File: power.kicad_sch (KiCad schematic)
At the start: 37 parts, among them Q1 SIS472DN-T1-GE3, Q2 SIS472DN-T1-GE3, Q3 AO3400A, U6 LM74700QDBVRQ1, U7 SIC431AED-T1-GE3, U8 LM74700QDBVRQ1, U9 TPS564247DRLR

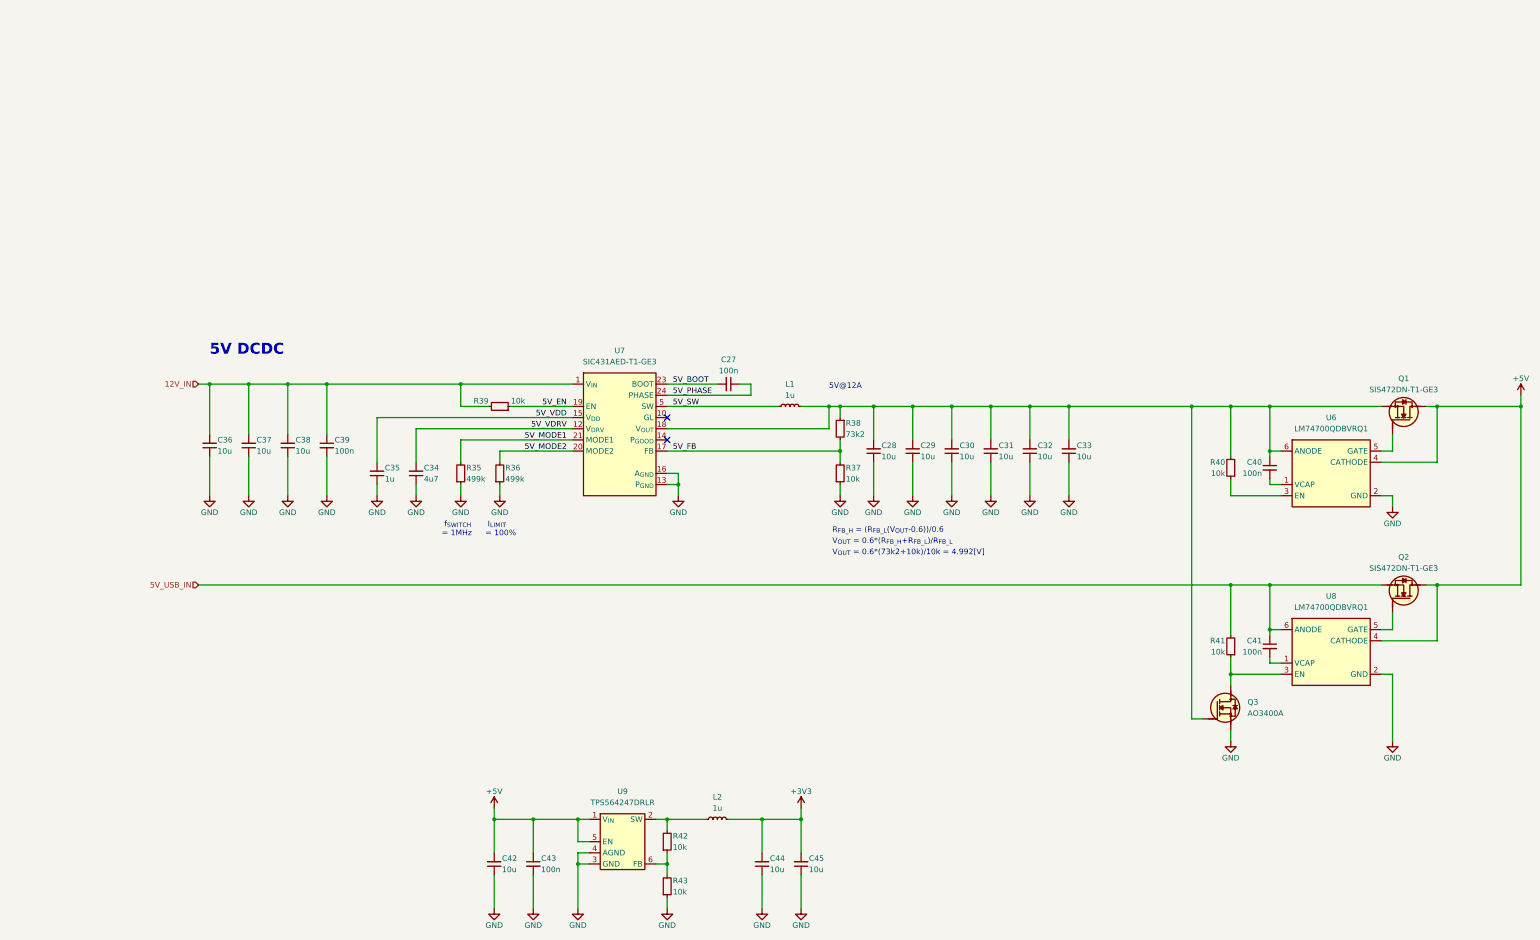
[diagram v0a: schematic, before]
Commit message: [#1] WIP: Refactor schematic
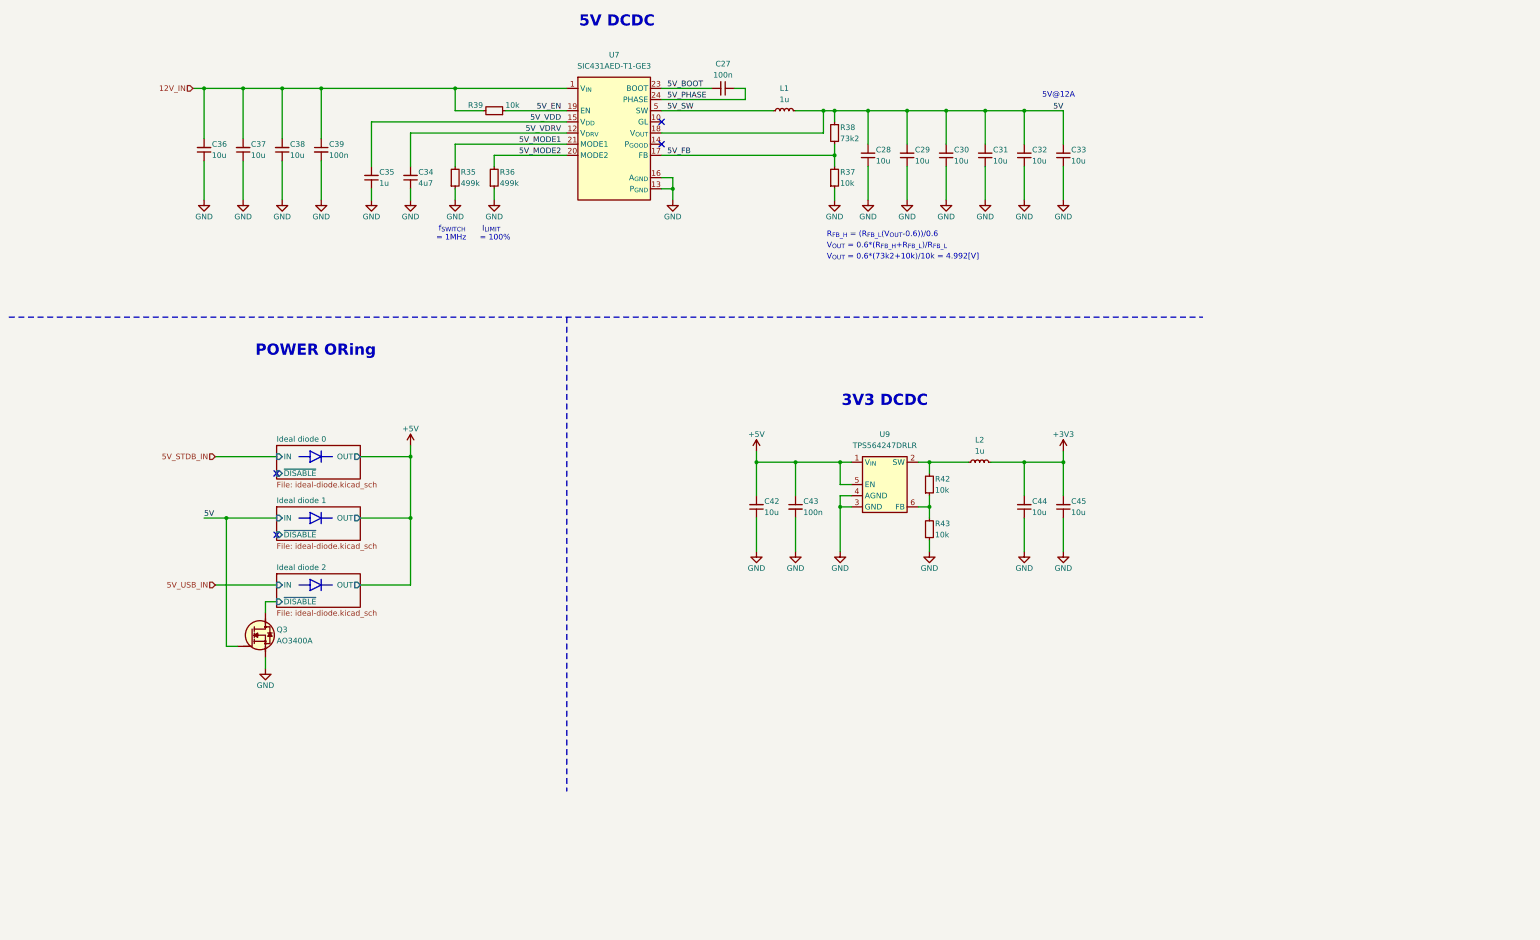
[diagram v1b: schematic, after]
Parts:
- removed C40, C41: C-100n-0402, DW-footprints:C_0402_1005Metric, symbol DW-capacitors:C-100n-0402
- removed Q1, Q2: SIS472DN-T1-GE3, DW-footprints:PowerPAK-1212-8_Single, symbol DW-transistors:SIS472DN-T1-GE3
- removed R40, R41: R-10k-0402, DW-footprints:R_0402_1005Metric, symbol DW-resistors:R-10k-0402
- removed U6, U8: LM74700QDBVRQ1, DW-footprints:SOT-23-6, symbol DW-ICs:LM74700QDBVRQ1
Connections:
- net 5V: now reaches C28.2, C29.2, C30.2, C31.2, C32.2, C33.2, L1.2, Q3.1 (G), R38.1, U7.18 (V_{OUT})
- net Ideal diode 2/~{DISABLE}: now reaches Q3.3 (D)
- no-connect marks 2 -> 4
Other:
- added sheet Ideal diode 0 (ideal-diode.kicad_sch)
- added sheet Ideal diode 1 (ideal-diode.kicad_sch)
- added sheet Ideal diode 2 (ideal-diode.kicad_sch)
- note added: "3V3 DCDC"
- note added: "POWER ORing"
- moved on the sheet: C27, C28, C29, C30, C31, C32, C33, C34, C35, C36, C37, C38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

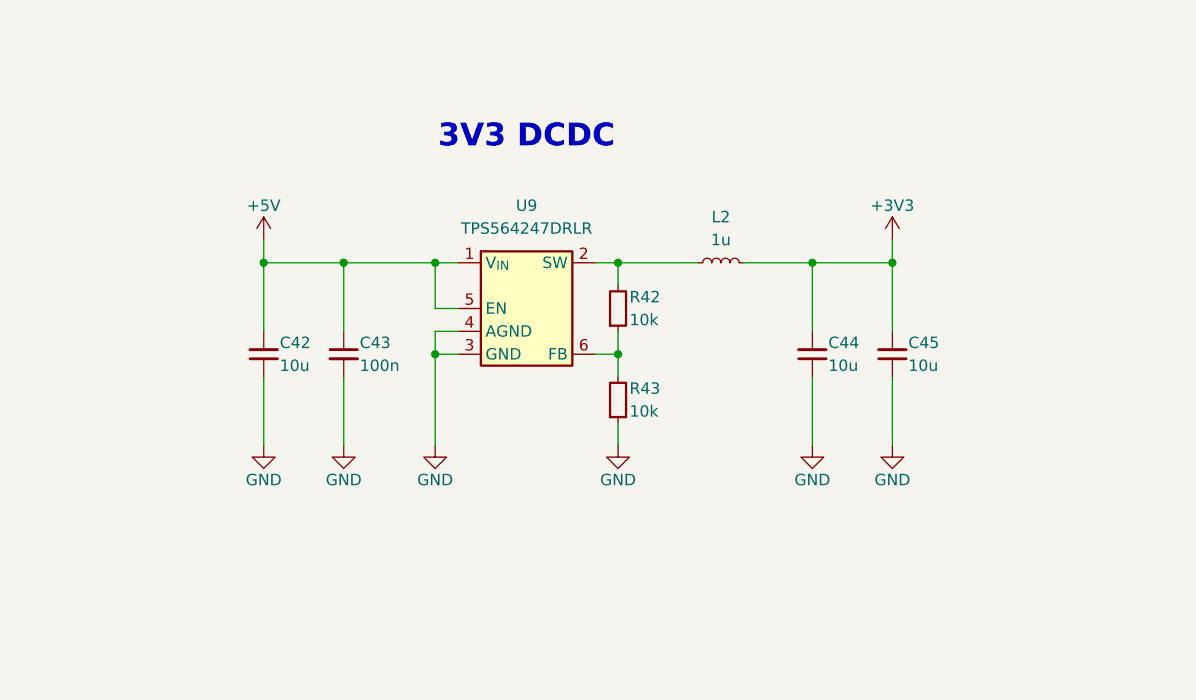
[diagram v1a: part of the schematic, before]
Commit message: [#1] Finish schematic design of the 3V3 DC-DC converter
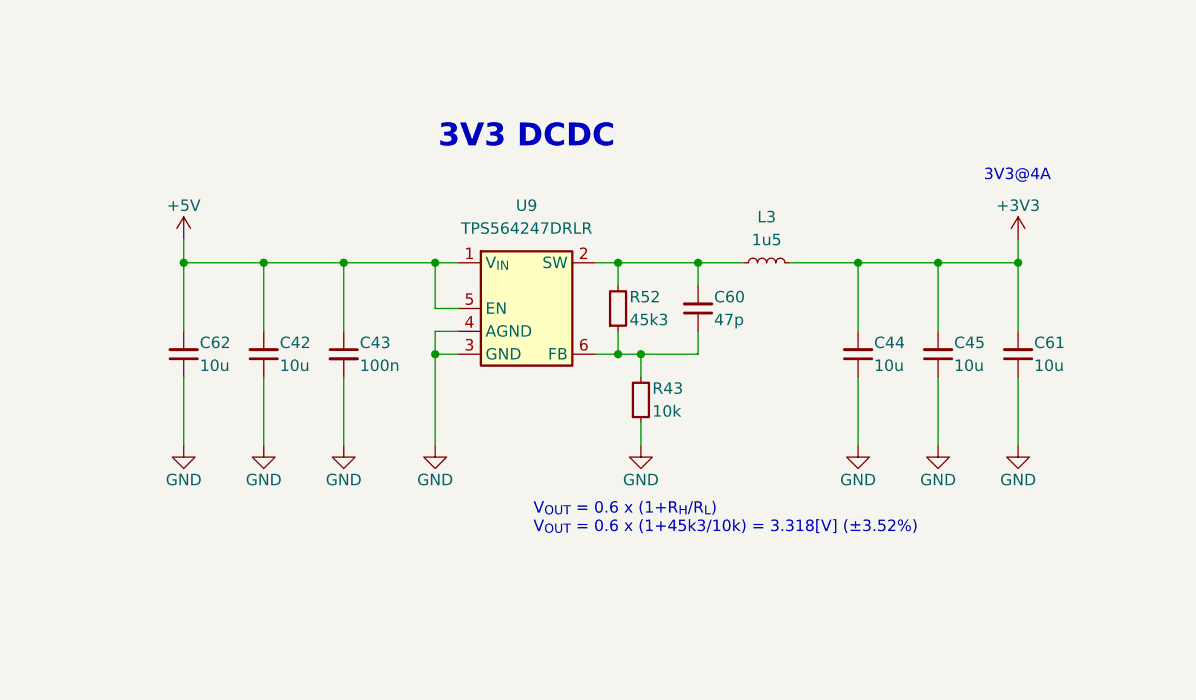
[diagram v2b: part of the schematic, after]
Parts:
- removed L2: L-1u-20A-CJiang-FEXL0650A, DW-footprints:L-CJiang-FEXL0650A, symbol DW-inductors:L-1u-20A-CJiang-FEXL0650A
- removed R42: R-10k-0402, DW-footprints:R_0402_1005Metric, symbol DW-resistors:R-10k-0402
- added C60: C-47p-0402, DW-footprints:C_0402_1005Metric, symbol DW-capacitors:C-47p-0402
- added C61, C62: C-10u-0603, DW-footprints:C_0603_1608Metric, symbol DW-capacitors:C-10u-0603
- added L3: L-1u5-6.5A-CJiang-FTC404030S, DW-footprints:L-CJiang-FTC404030S, symbol DW-inductors:L-1u5-6.5A-CJiang-FTC404030S
- added R52: R-45k3-0402, DW-footprints:R_0402_1005Metric, symbol DW-resistors:R-45k3-0402
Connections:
- net +3V3: now also C61.2, L3.2
- net +5V: now also C62.2
- net GND: now also C61.1, C62.1
- net at R43.2, U9.6 (FB): now also C60.1, R52.1
- net at U9.2 (SW): now also C60.2, L3.1, R52.2
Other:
- note added: "3V3@4A"
- note added: "V_{OUT} = 0.6 x (1+R_{H}/R_{L}) V_{OUT} = 0.6 x (1+45k3/10k) = 3.318[V] (±3.52%)"
- moved on the sheet: C44, C45, R43

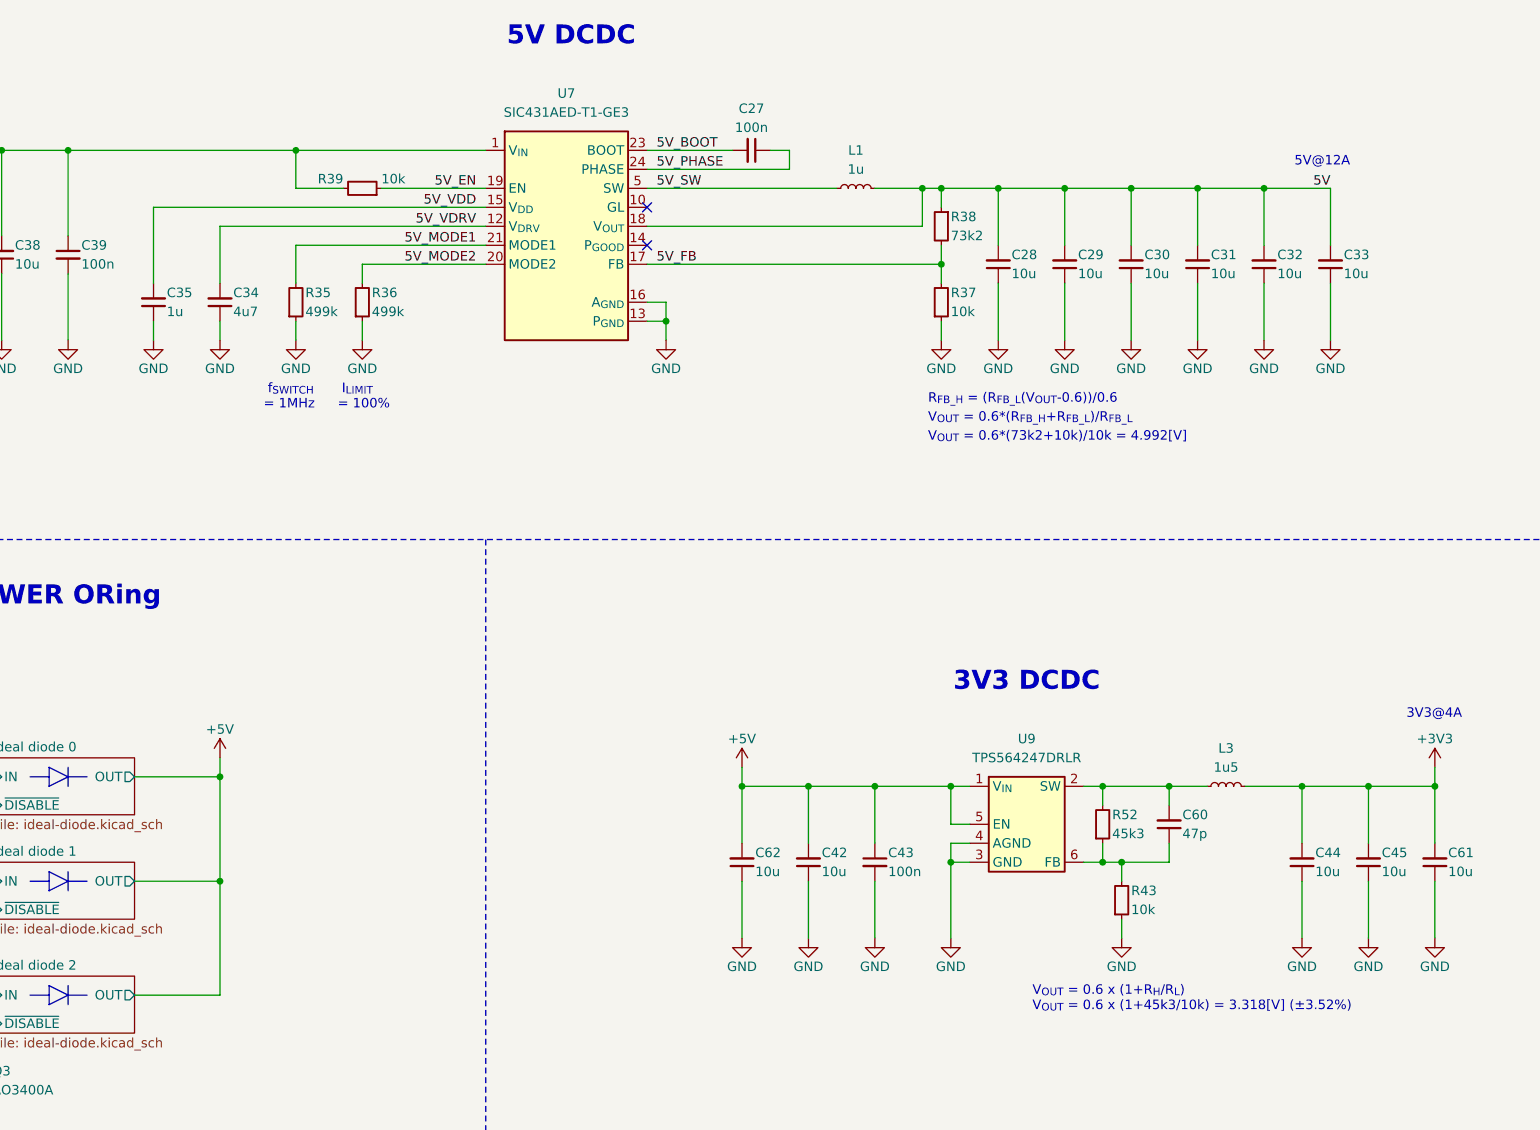
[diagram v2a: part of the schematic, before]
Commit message: [#1] Add USB to CAN schematic, add power flags to 5V and 3V3
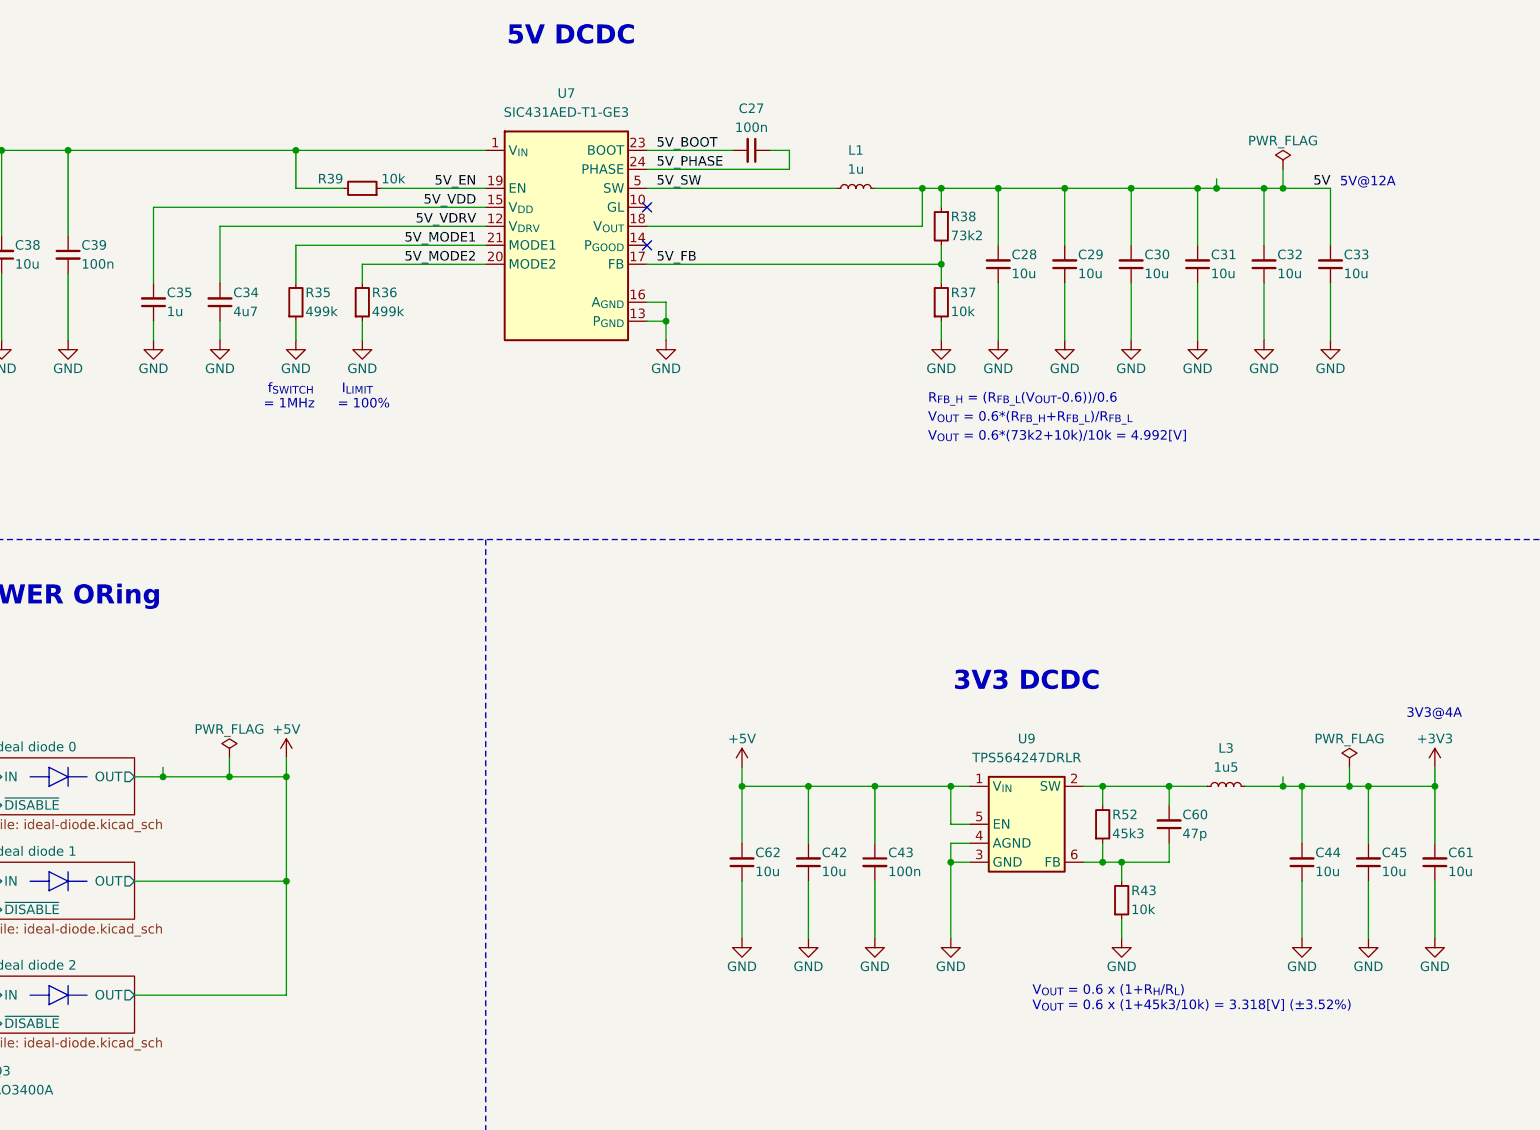
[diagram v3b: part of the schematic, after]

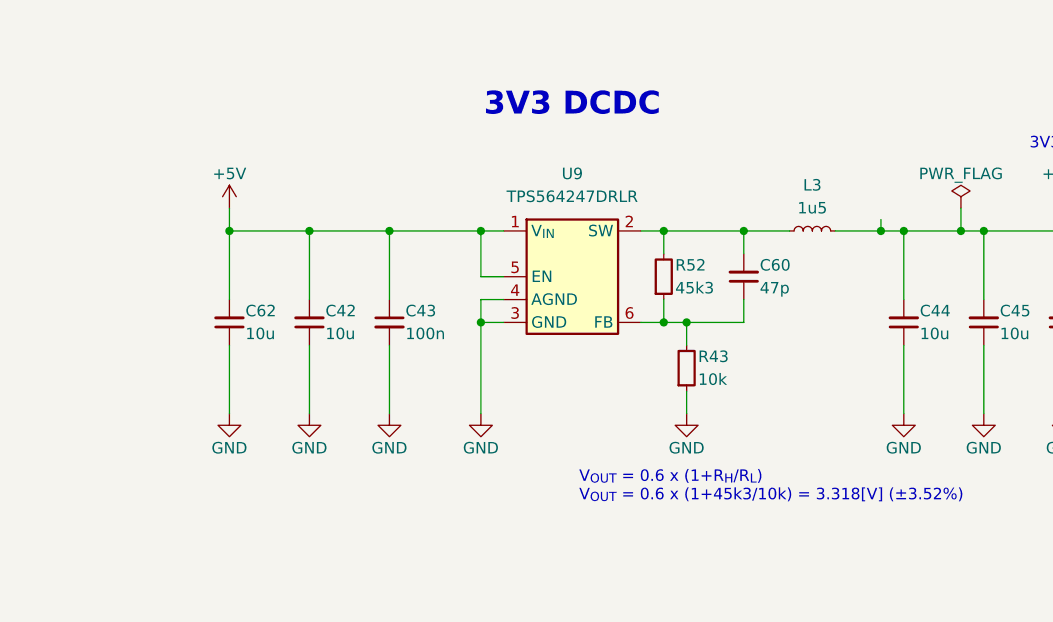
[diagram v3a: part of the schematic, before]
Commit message: [#3] Fix 3V3 DC-DC converter schematic, change one USB-C to a vertical one, start layout
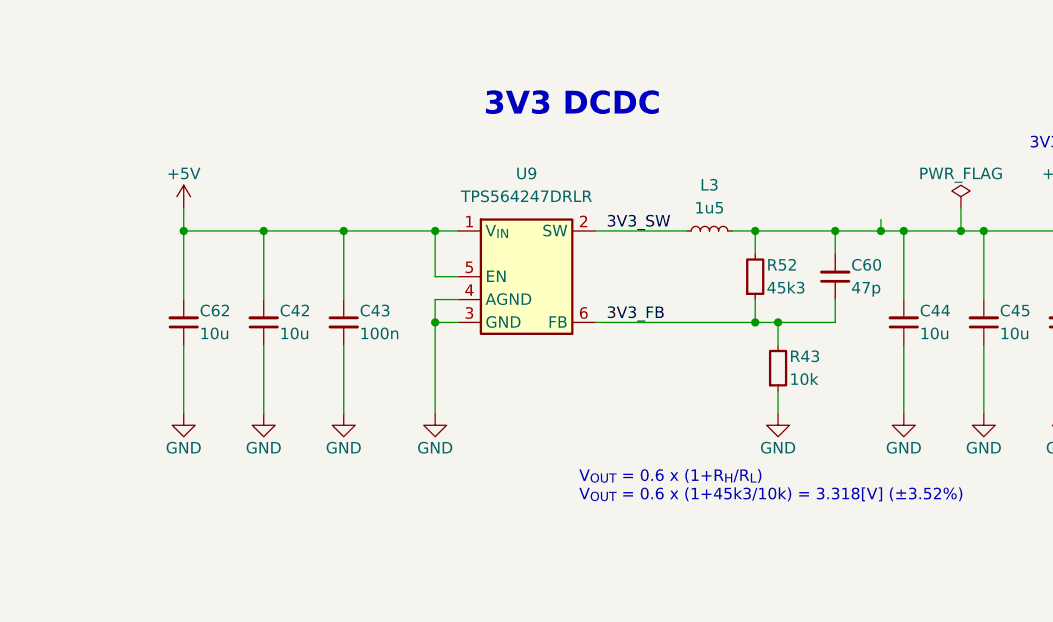
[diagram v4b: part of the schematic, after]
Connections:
- net +3V3: now also C60.2, R52.2
- net 3V3_FB: now reaches C60.1, R43.2, R52.1, U9.6 (FB)
- net 3V3_SW: now reaches L3.1, U9.2 (SW)
- net 3V3_SW: no longer C60.2, R52.2
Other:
- moved on the sheet: C42, C43, C60, C62, L3, R43, R52, U9
